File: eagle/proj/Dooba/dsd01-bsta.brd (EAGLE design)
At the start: 85.3 x 70.1 mm, 63 parts, among them J1 PWRJACK5521, J8 ARJC02-111008B, P1 DIO, P2 CKI-CKO, P3 NOT, P4 RDY, P5 PWR(VIN-GND-RST), P6 SWD_CORE(SWCLK-SWDIO-GND), P7 SWD_CORE(SWCLK-SWDIO-GND), P8 SWD(GND-RST)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

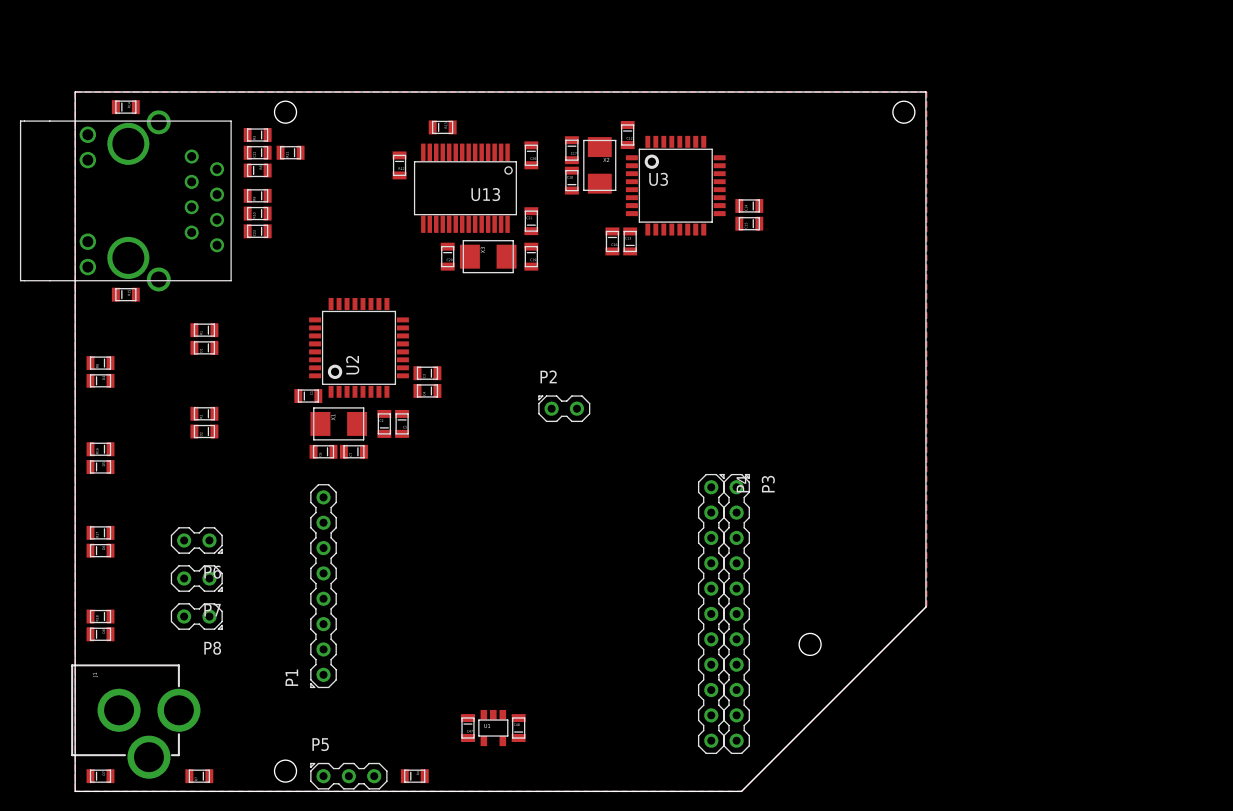
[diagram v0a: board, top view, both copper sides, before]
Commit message: Routed DSD01-BSTA
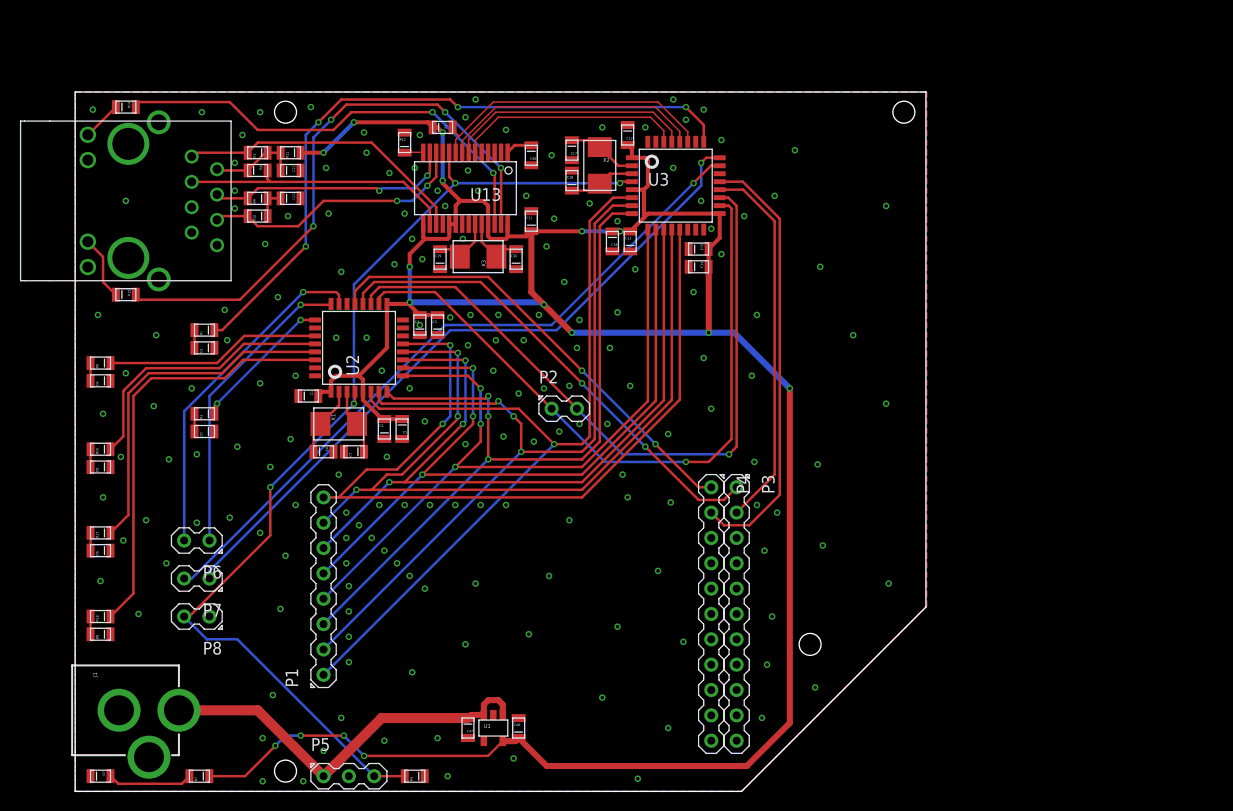
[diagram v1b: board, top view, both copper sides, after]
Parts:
- moved C19 9.15 mm to (41.4, 55.4), turned to 270 degrees
- moved C14 7.94 mm to (67.3, 54.6), turned to 180 degrees
- moved C20 6.86 mm to (49.0, 55.4), turned to 270 degrees
- moved C4 6.65 mm to (39.4, 48.8), turned to 270 degrees
- moved C15 5.68 mm to (67.3, 56.4), turned to 180 degrees
- moved C3 4.93 mm to (41.1, 48.8), turned to 270 degrees
- moved C23 4.67 mm to (26.4, 61.5), turned to 180 degrees
- moved C22 3.75 mm to (26.4, 64.3), turned to 180 degrees
- moved R12 2.34 mm to (37.8, 67.1), turned to 270 degrees
- moved R3 1.78 mm to (23.1, 66.0)
- moved X3 1.02 mm to (45.2, 55.6), turned to 180 degrees
- moved C2 0.51 mm to (35.8, 38.4)
- moved C5 0.51 mm to (37.6, 38.4)
- moved R10 0.25 mm to (23.1, 59.7)
- moved R9 0.25 mm to (23.1, 61.5)
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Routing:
- net VCC: track 0.00 -> 268.7 mm, vias 0 -> 16
- net N$24: track 0.00 -> 106.1 mm, vias 0 -> 4
- net N$15: track 0.00 -> 84.4 mm, vias 0 -> 1
- net N$12: track 0.00 -> 83.3 mm, vias 0 -> 2
- net N$6: track 0.00 -> 81.1 mm, vias 0 -> 3
- net N$11: track 0.00 -> 80.8 mm, vias 0 -> 3
- net N$10: track 0.00 -> 78.4 mm, vias 0 -> 3
- net N$7: track 0.00 -> 77.5 mm, vias 0 -> 3
- net N$9: track 0.00 -> 77.4 mm, vias 0 -> 3
- net N$8: track 0.00 -> 75.1 mm, vias 0 -> 3
- net N$13: track 0.00 -> 71.3 mm, vias 0 -> 1
- net N$42: track 0.00 -> 70.8 mm, vias 0 -> 1
- net N$51: track 0.00 -> 70.4 mm, vias 0 -> 1
- net N$14: track 0.00 -> 68.6 mm, vias 0 -> 1
- net N$56: track 0.00 -> 67.9 mm, vias 0 -> 4
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
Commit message: Completed DSY01 & DSD01-BSTA boards
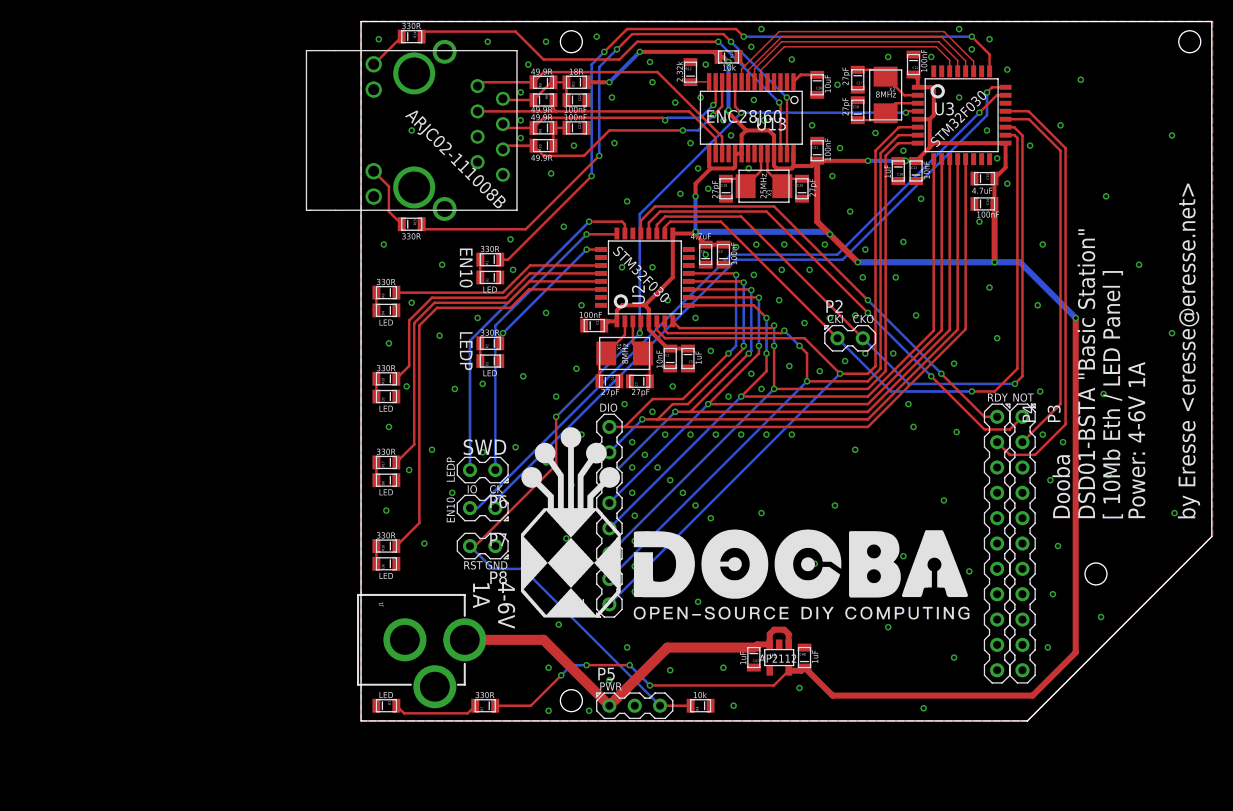
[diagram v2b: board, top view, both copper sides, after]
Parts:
- C19, C20: value 15pF -> 27pF
- R14, R15: value 220R -> 330R
- moved C13 29.5 mm to (89.1, 64.2)
- moved D5 29.5 mm to (36.0, 41.6)
- moved R12 29.5 mm to (66.5, 74.1)
- moved U1 29.5 mm to (75.4, 15.4)
- moved C15 29.5 mm to (96.0, 63.4)
- moved C16 29.5 mm to (87.3, 64.2)
- moved C17 29.5 mm to (83.3, 73.4)
- moved C18 29.5 mm to (83.3, 70.3)
- moved C19 29.5 mm to (70.1, 62.4)
- moved C47 29.5 mm to (72.8, 15.4)
- moved C5 29.5 mm to (66.2, 45.4)
- moved C7 29.5 mm to (61.4, 43.1)
- moved D4 29.5 mm to (36.0, 50.2)
- moved D6 29.5 mm to (36.0, 33.2)
- moved D7 29.5 mm to (36.0, 10.6)
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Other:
- board text added: "100nF"
- board text added: "10k"
- board text added: "10nF"
- board text added: "10uF"
- board text added: "18R"
- board text added: "1uF"
- board text added: "2.32k"
- board text added: "25MHz"
- board text added: "27pF"
- board text added: "330R"
- board text added: "4-6V 1A"
- board text added: "4.7uF"
- board text added: "49.9R"
- board text added: "8MHz"
- board text added: "AP2112"
- board text added: "ARJC02-111008B"
- board text added: "CK"
- board text added: "CKI"
- board text added: "CKO"
- board text added: "DIO"
- board text added: "Dooba DSD01-BSTA "Basic Station" [ 10Mb Eth / LED Panel ] Power: 4-6V 1A by Eresse <eresse@eresse.net>"
- board text added: "EN10"
- board text added: "ENC28J60"
- board text added: "GND"
- board text added: "IO"
- board text added: "LED"
- board text added: "LEDP"
- board text added: "NOT"
- board text added: "PWR"
- board text added: "RDY"
- board text added: "RST"
- board text added: "STM32F030"
- board text added: "SWD"
